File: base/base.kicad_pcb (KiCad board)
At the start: 4 copper layers, 30 x 90 mm, 6 parts, among them J1 DF40GB(1.5)-30DS-0.4V(51), J2 DIP-48_Socket

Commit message: wip: snapshot base board before connector/socket rework
Safety commit taken before swapping the mezzanine connector and the
DIP48 socket. No design intent here beyond preserving the tree.

Co-Authored-By: Claude Opus 5 <noreply@anthropic.com>
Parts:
- moved R2 0.70 mm to (112.3, 107.9)
- moved C1 0.31 mm to (112.3, 90.8)
- moved C2 0.31 mm to (112.3, 89.0)
- moved R1 0.09 mm to (112.3, 77.3)
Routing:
- net //WE: track 129.8 -> 16.6 mm
- net VCC: track 154.7 -> 65.3 mm, vias 1 -> 2
- net /RY//BY: track 37.7 -> 22.0 mm
- net //RE: track 20.7 -> 16.1 mm
- net /IO1: track 30.2 -> 25.8 mm
- net /IO2: track 28.1 -> 24.7 mm
- net /IO4: track 21.3 -> 19.6 mm
- net /IO7: track 16.8 -> 17.9 mm
- net /ALE: track 19.5 -> 20.1 mm
- net GND: vias 175 -> 173
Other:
- board text added: "VFBGA67 to ZIF48"

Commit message: Route base for the 4.0mm mezzanine and the SMT DIP48 field
Copper follow-up to f02e7d7, which changed only symbols, schematics and
footprints. Both boards now carry the new parts.

carrier: J1 swapped to DF40TC-30DP-0.4V(51). All 30 signal pads landed on
their exact previous coordinates, so nothing was re-routed; the four G1-G4
retention-tab pads are gone. 0 DRC violations, 0 unconnected. Panel
regenerated.

base: J1 swapped to DF40TC(4.0)-30DS-0.4V(51), same story. J2 swapped to
the surface-mount socket-strip field; its 48 pads keep their Y coordinates
and stagger +-1.65 mm about the unchanged row centrelines.

The interesting part is what SMD pads cost. They live on F.Cu only, and
this board's copper arrived at the old through-hole pads from all four
layers -- F.Cu on 4 pins, B.Cu on 7, In1 on 6, In2 on 3. Rather than
re-plan the whole board, route_base.py now gives every used J2 pad a
0.15 mm F.Cu stub back to its row centreline and a 0.45/0.20 via there.
The via sits exactly where the through-hole pad centre used to be, which
is the coordinate every existing route and the planner already target. 19
pads, and connectivity came back without moving a single destination.
The 1.4 mm gap between the staggered pad columns takes that via with
0.475 mm of copper clearance against a 0.1 mm rule.

Also in route_base.py: VCC now falls back from J2.37 to J2.12, and pin 10
routes before pin 6 so pin 6 can be offered pin 10's via.

The four passives moved 0.5 mm left with their track endpoints. They were
placed against a through-hole field whose copper started 1.8 mm further
right; the SMT pads brought J2's copper out to x=113.88 and the 0603
courtyards overlapped it. Copper clearance was still legal at 0.168 mm --
this was a courtyard fix, not an electrical one.

base is 0 DRC violations, 6 unconnected, both understood and documented
in HANDOFF:
  - J1.6 (VCC) is walled in on B.Cu by IO5's and IO7's hand routes, which
    pass 0.4 mm away -- exactly the via limit -- leaving i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
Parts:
- J1: value DF40GB(1.5)-30DS-0.4V(51) -> DF40TC(4.0)-30DS-0.4V(51); footprint Connector_Hirose_DF40:HIROSE_DF40GB-30DS-0.4V_51_ -> Connector_Hirose_DF40:HIROSE_DF40TC_4.0_-30DS-0.4V_51_
- J2: value DIP-48_Socket -> DIP-48_SocketStrip_SMD; footprint base:DIP-48_Socket_W15.24mm_P2.54mm -> base:DIP-48_SocketStrip_SMD_W15.24mm_P2.54mm
- moved C1 0.50 mm to (111.8, 90.8)
- moved C2 0.50 mm to (111.8, 89.0)
- moved R1 0.50 mm to (111.8, 77.3)
- moved R2 0.50 mm to (111.8, 107.9)
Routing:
- net VCC: track 65.3 -> 220.6 mm, vias 2 -> 3
- net /RY//BY: track 22.0 -> 60.3 mm, vias 0 -> 1
- net //WE: track 16.6 -> 48.5 mm, vias 0 -> 2
- net //CE: track 20.7 -> 45.9 mm, vias 1 -> 2
- net GND: track 0.00 -> 23.1 mm, vias 173 -> 171
- net /ALE: track 20.1 -> 38.6 mm, vias 1 -> 2
- net /IO1: track 25.8 -> 41.2 mm, vias 1 -> 2
- net /IO4: track 19.6 -> 34.4 mm, vias 1 -> 2
- net //WP: track 30.2 -> 44.7 mm, vias 1 -> 2
- net //RE: track 16.1 -> 30.5 mm, vias 1 -> 2
- net /IO3: track 23.1 -> 37.1 mm, vias 1 -> 2
- net /IO2: track 24.7 -> 38.0 mm, vias 1 -> 2
- net /IO8: track 21.6 -> 33.2 mm, vias 0 -> 1
- net /IO7: track 17.9 -> 29.5 mm, vias 0 -> 1
- net /IO6: track 17.9 -> 29.5 mm, vias 0 -> 1
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
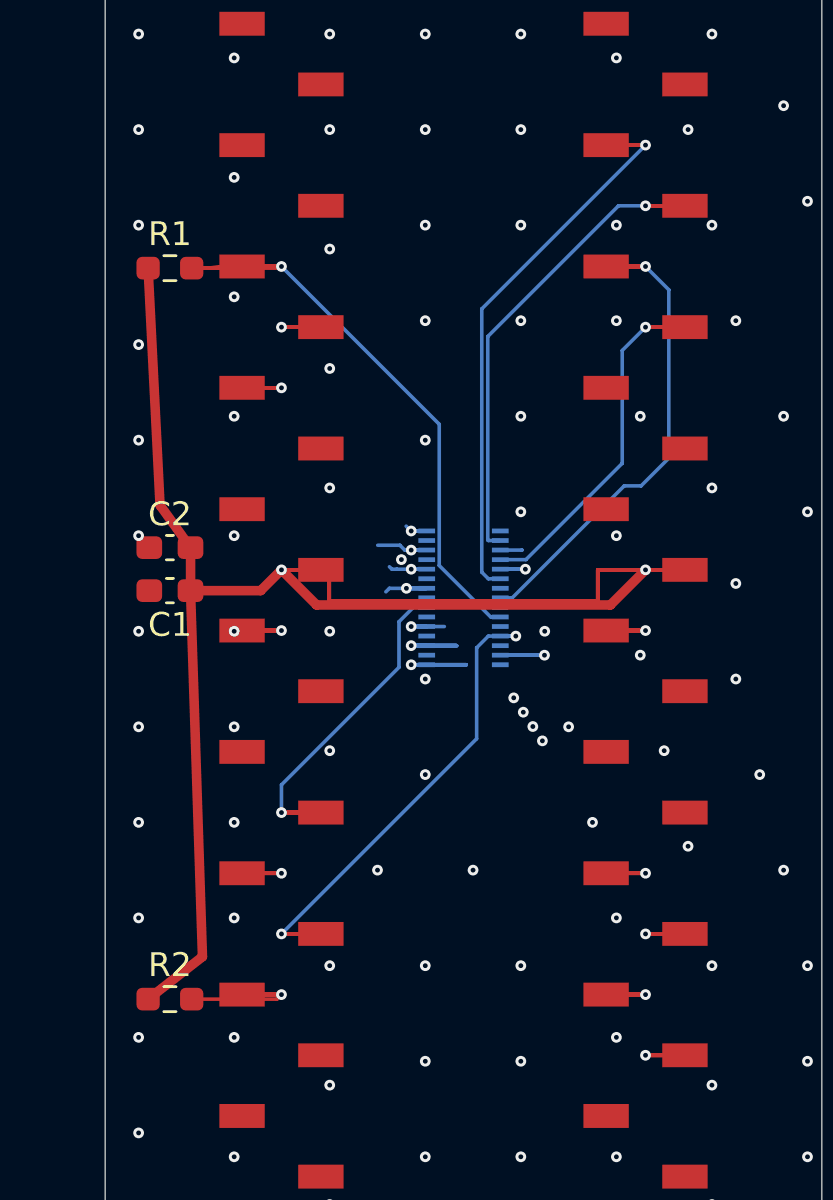
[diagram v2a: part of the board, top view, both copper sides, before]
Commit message: base: hand routing closes J1.6; 3 unconnected left, all pour fragments
Alex's routing pass on base/base.kicad_pcb, plus the doc corrections it
implies.

Board state: 0 DRC violations, 3 unconnected, down from 6. ERC clean.
Verified independently of DRC that every connector pad is actually
connected: all 19 used J2 pads have a track endpoint on the pad centre,
and the 13 J1 pads with no track are exactly the checkerboard's GND pins,
which take the pour by design.

J1.6 (VCC) is routed. It escapes *inward* on B.Cu -- a 0.5 mm stub from
(125.14, 89.103) into the channel between the connector rows. That is the
direction tools/route_base.py rejects: outward there is no via position
because IO5's and IO7's routes sit 0.4 mm away, exactly the via clearance
limit, and inward its stub check fails. So this route is hand work the
router cannot recreate. strip() preserves F.Cu and B.Cu, so a rerun of
make route-base leaves it alone, but it is worth checking afterwards --
noted in both README and HANDOFF.

Copper is down from 342 tracks / 802 mm to 125 tracks / 387 mm, with more
of the work moved onto In1.Cu. Footprints, board outline and placement are
unchanged from e93e175.

Remaining 3 unconnected are detached GND pour fragments, the same class as
before and two fewer. They are the only reason make check reports
base drc FAIL: no shorts, no clearance violations, no missing connections.

Co-Authored-By: Claude Opus 5 <noreply@anthropic.com>
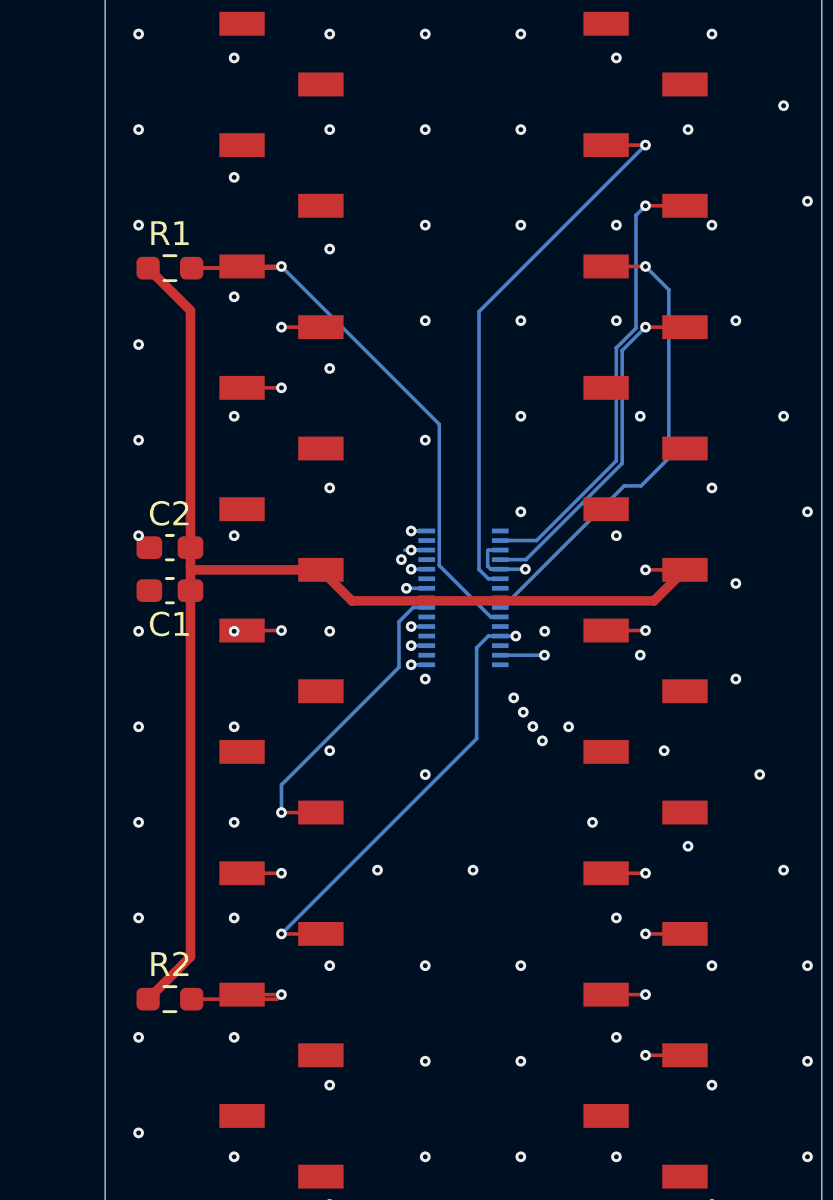
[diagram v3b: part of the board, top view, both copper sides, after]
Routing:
- net VCC: track 220.6 -> 63.4 mm, vias 3 -> 2
- net /RY//BY: track 60.3 -> 27.9 mm
- net //CE: track 45.9 -> 19.3 mm
- net /ALE: track 38.6 -> 14.1 mm
- net //WP: track 44.7 -> 22.2 mm
- net GND: track 23.1 -> 3.30 mm
- net /IO1: track 41.2 -> 26.4 mm
- net /IO2: track 38.0 -> 24.2 mm
- net /IO3: track 37.1 -> 23.3 mm
- net //RE: track 30.5 -> 17.1 mm
- net //WE: track 48.5 -> 35.4 mm
- net /IO4: track 34.4 -> 21.3 mm
- net /IO7: track 29.5 -> 19.1 mm
- net /IO6: track 29.5 -> 19.6 mm
- net /IO5: track 24.4 -> 14.5 mm
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
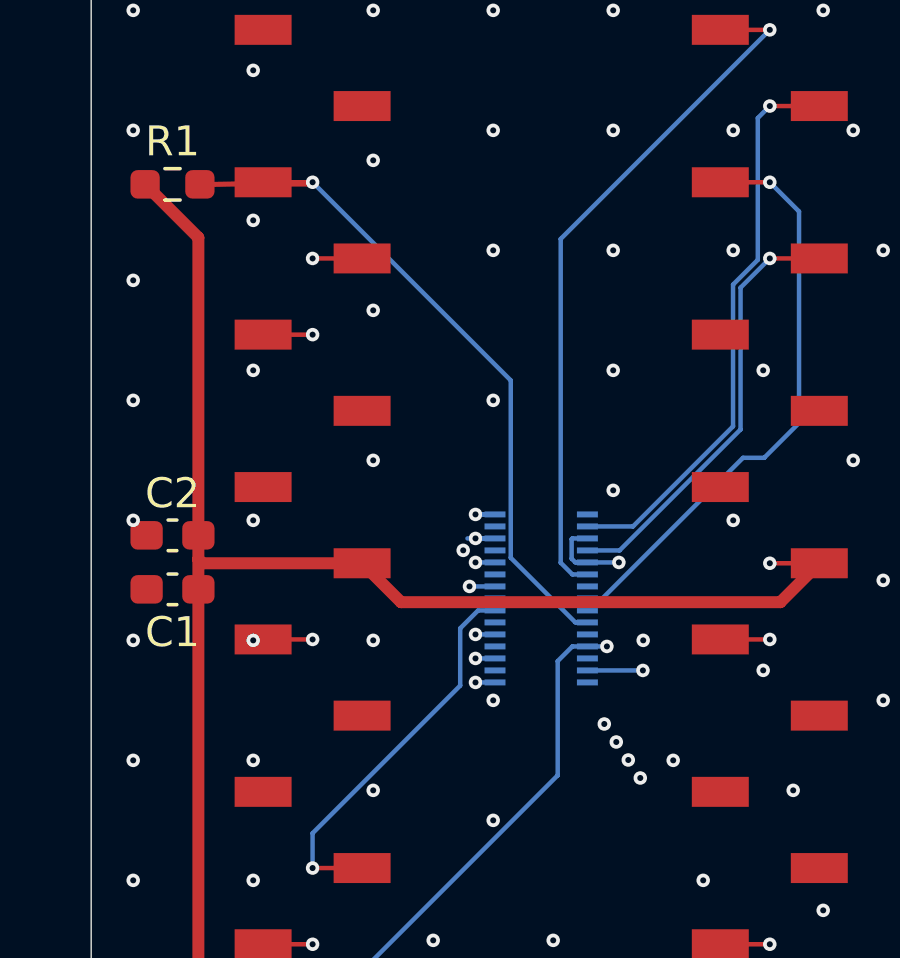
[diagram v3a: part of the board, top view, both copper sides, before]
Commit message: base is clean: 0 DRC violations, 0 unconnected
Alex's second routing pass closes the last of it. make check now passes on
both projects for the first time.

The fix was four edits on B.Cu, +1 track and +0.2 mm of copper:

  added    GND  (121.5, 89.5) -> (122.56, 89.502)
  moved    RY//BY diagonal from x=123.085 to x=123.55
  moved    /WE corner from 125.14 to 125.097
  removed  /IO3 stub at y=89.103

The GND segment is the interesting one. The three detached pour fragments
were not slivers wanting another stitching via, which is what
tie_fragments kept trying -- and why more rounds made it worse rather than
better. The pour needed one direct tie to a J1 GND pad. Noted in both
README and HANDOFF in case fragments come back after a re-pour.

Checked rather than assumed, since a deleted signal track is exactly the
edit that can silently open a net:
  - pad -> net mapping byte-identical across all 86 pads
  - footprints unchanged: part, position, layer, rotation
  - board outline unchanged at 30.05 x 90.05, via count unchanged at 197
  - all 19 used J2 pads have a track endpoint on the pad centre
  - J1's 12 unlanded pads are exactly the checkerboard's GND pins
  - KiCad's own connectivity engine agrees with DRC: GetUnconnectedCount 0

So /IO3 survives its reroute end to end despite losing that stub.

Docs record the two routes route_base.py cannot reproduce -- J1.6's inward
escape and the GND pad tie -- because strip() preserves F.Cu and B.Cu and
a rerun will silently leave them out if they are ever lost.

Co-Authored-By: Claude Opus 5 <noreply@anthropic.com>
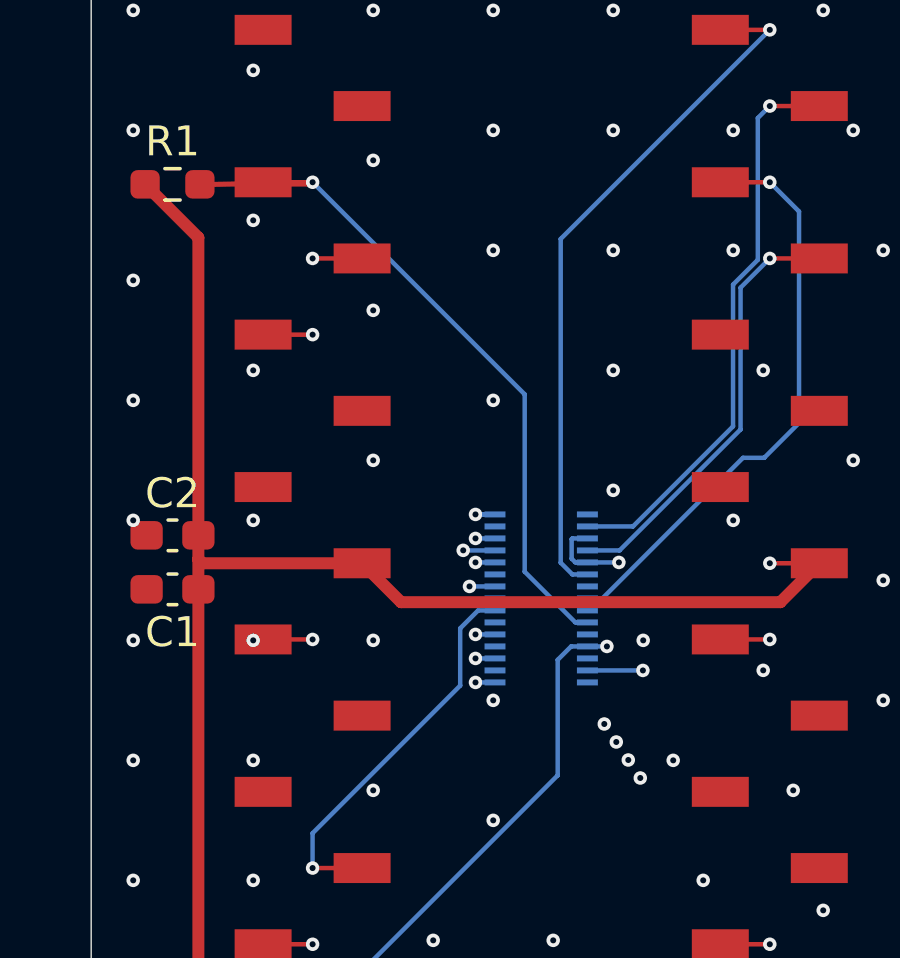
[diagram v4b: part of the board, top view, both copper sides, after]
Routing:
- net GND: track 3.30 -> 4.36 mm
- net /IO3: track 23.3 -> 22.4 mm
